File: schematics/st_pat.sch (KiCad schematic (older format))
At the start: 20 parts, among them J4 BATTERY, SW1 SW_PWR, SW2 BTN_RST, SW3 BTN, SW4 BTN, SW5 BTN, U1 FGPMMOPA6H, U2 FEATHER_M0_BASIC_PROTO, U3 LIS2MDL_ADAFRUIT, U4 Sharp_Display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

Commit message: add sharp display number to schematic
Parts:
- U4: value Sharp_Display -> Sharp_Display_4694; symbol st_pat:Sharp_Display -> st_pat:Sharp_Display_4694
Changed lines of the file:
@@
 NoConn ~ 4750 4700
 $Comp
-L st_pat:Sharp_Display U4
+L st_pat:Sharp_Display_4694 U4
 U 1 1 602ACB65
 P 8900 1750
 F 0 "U4" H 9125 1865 50  0000 C CNN
-F 1 "Sharp_Display" H 9125 1774 50  0000 C CNN
+F 1 "Sharp_Display_4694" H 9125 1774 50  0000 C CNN
 F 2 "st_pat:Sharp_Display" H 8900 1750 50  0001 C CNN
 F 3 "" H 8900 1750 50  0001 C CNN

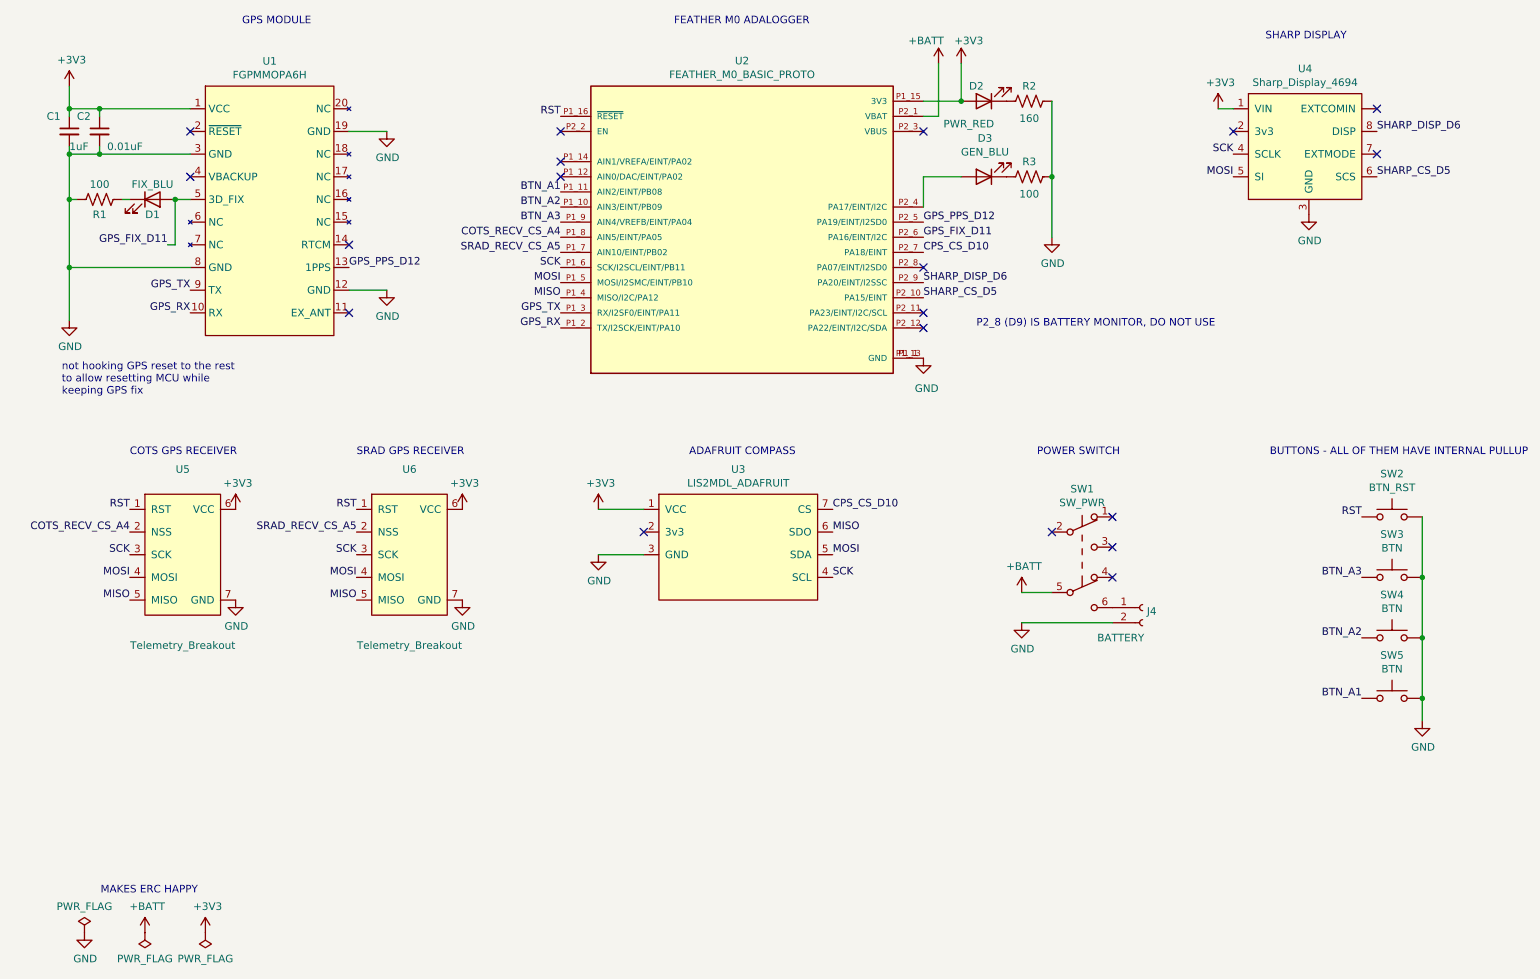
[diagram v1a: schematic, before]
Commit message: add power estimate to each component
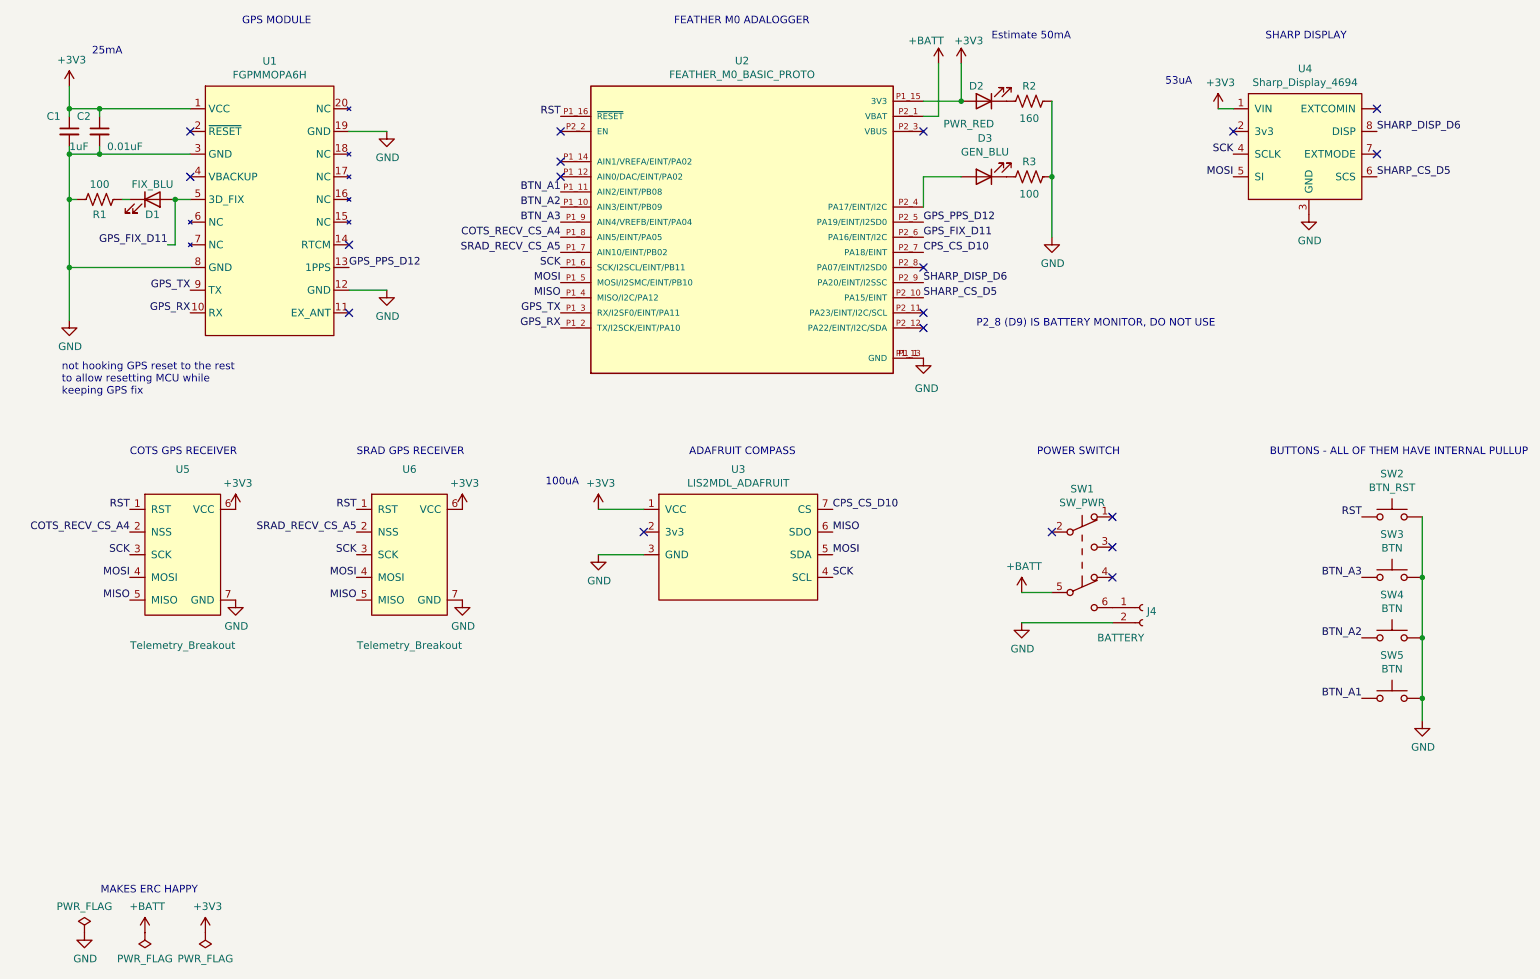
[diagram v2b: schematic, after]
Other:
- note added: "100uA"
- note added: "25mA"
- note added: "53uA"
- note added: "Estimate 50mA"
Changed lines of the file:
@@
 Text Notes 6950 3350 0    50   ~ 0
 P2_8 (D9) IS BATTERY MONITOR, DO NOT USE
+Text Notes 1100 1550 0    50   ~ 0
+25mA
+Text Notes 7050 1450 0    50   ~ 0
+Estimate 50mA
+Text Notes 8200 1750 0    50   ~ 0
+53uA
+Text Notes 4100 4400 0    50   ~ 0
+100uA
 $EndSCHEMATC

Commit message: fix pr issues
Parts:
- U5: value Telemetry_Breakout -> COTS_GPS_RECEIVER
- U6: value Telemetry_Breakout -> SRAD_GPS_RECEIVER
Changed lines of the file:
@@
 P 1700 4350
 F 0 "U5" H 1700 4415 50  0000 C CNN
-F 1 "Telemetry_Breakout" H 1700 3250 50  0000 C CNN
+F 1 "COTS_GPS_RECEIVER" H 1700 3250 50  0000 C CNN
 F 2 "st_pat:Telemetry_Breakout" H 1700 4350 50  0001 C CNN
 F 3 "" H 1700 4350 50  0001 C CNN
@@
 P 3200 4350
 F 0 "U6" H 3200 4415 50  0000 C CNN
-F 1 "Telemetry_Breakout" H 3200 3250 50  0000 C CNN
+F 1 "SRAD_GPS_RECEIVER" H 3200 3250 50  0000 C CNN
 F 2 "st_pat:Telemetry_Breakout" H 3200 4350 50  0001 C CNN
 F 3 "" H 3200 4350 50  0001 C CNN

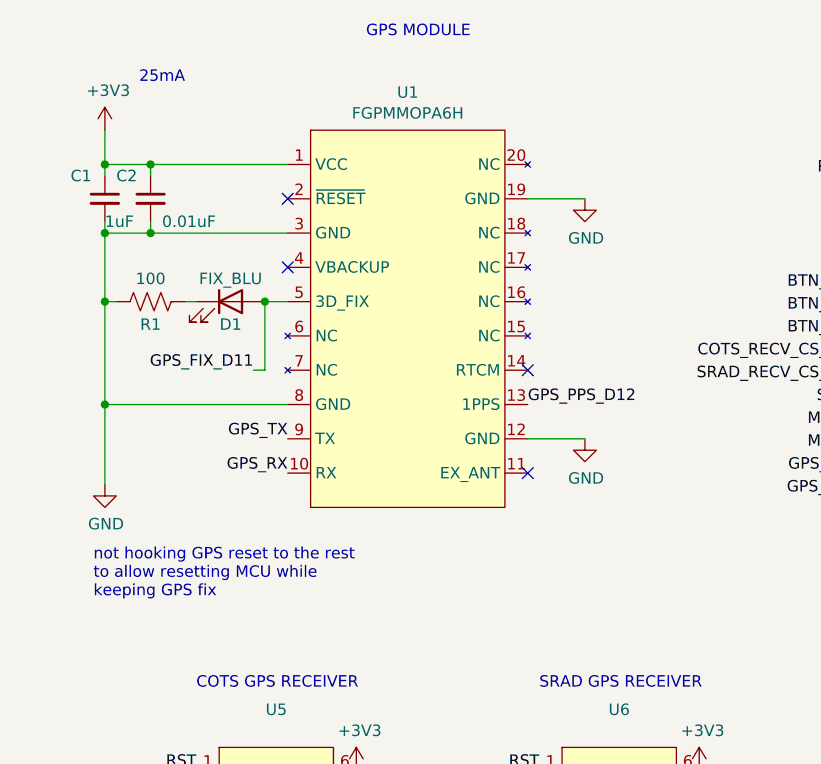
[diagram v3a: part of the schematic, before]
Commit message: wip replacing gps module with breakout
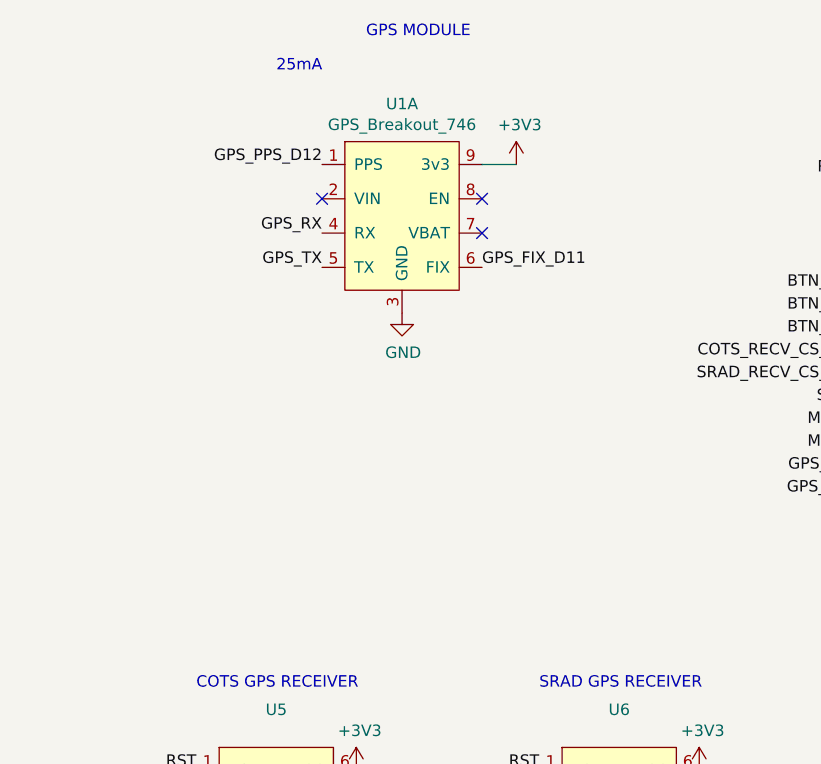
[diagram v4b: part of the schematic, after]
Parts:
- removed C1: 1uF, Capacitor_SMD:C_0805_2012Metric_Pad1.18x1.45mm_HandSolder, symbol Device:C_Small
- removed C2: 0.01uF, Capacitor_SMD:C_0805_2012Metric_Pad1.18x1.45mm_HandSolder, symbol Device:C_Small
- removed D1: FIX_BLU, LED_SMD:LED_1206_3216Metric_Pad1.42x1.75mm_HandSolder, symbol Device:LED
- removed R1: 100, Resistor_SMD:R_0805_2012Metric_Pad1.20x1.40mm_HandSolder, symbol Device:R_US
- removed U1: FGPMMOPA6H, st_pat:FGPMMOPA6H, symbol st_pat:FGPMMOPA6H
- added U1: GPS_Breakout_746, st_pat:GPS_Breakout_746, symbol st_pat:GPS_Breakout_746
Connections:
- net +3V3: now also U1.9 (3v3)
- net GND: now also U1.3 (GND)
- net GPS_FIX_D11: now also U1.6 (FIX)
- net GPS_PPS_D12: now also U1.1 (PPS)
- net GPS_RX: now also U1.4 (RX)
- net GPS_TX: now also U1.5 (TX)
- no-connect marks 19 -> 18
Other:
- note removed: "not hooking GPS reset to the rest\nto allow resetting MCU while\nkeeping GPS fix"
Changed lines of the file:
@@
 Comment4 ""
 $EndDescr
-$Comp
-L st_pat:FGPMMOPA6H U1
-U 1 1 600D122C
-P 2200 1650
-F 0 "U1" H 2275 1715 50  0000 C CNN
-F 1 "FGPMMOPA6H" H 2275 1624 50  0000 C CNN
-F 2 "st_pat:FGPMMOPA6H" H 2200 1650 50  0001 C CNN
-F 3 "https://cdn-shop.adafruit.com/datasheets/GlobalTop-FGPMMOPA6H-Datasheet-V0A.pdf" H 2200 1650 50  0001 C CNN
-	1    2200 1650
-	1    0    0    -1
-$EndComp
 Text Notes 9400 1450 2    50   ~ 0
 SHARP DISPLAY
@@
 L power:+3V3 #PWR01
 U 1 1 60185239
-P 950 1750
-F 0 "#PWR01" H 950 1600 50  0001 C CNN
-F 1 "+3V3" H 965 1923 50  0000 C CNN
-F 2 "" H 950 1750 50  0001 C CNN
-F 3 "" H 950 1750 50  0001 C CNN
-	1    950  1750
+P 2750 1900
+F 0 "#PWR01" H 2750 1750 50  0001 C CNN
+F 1 "+3V3" H 2765 2073 50  0000 C CNN
+F 2 "" H 2750 1900 50  0001 C CNN
+F 3 "" H 2750 1900 50  0001 C CNN
+	1    2750 1900
 	1    0    0    -1
 $EndComp
@@
 L power:GND #PWR03
 U 1 1 60187238
-P 950 3300
-F 0 "#PWR03" H 950 3050 50  0001 C CNN
-F 1 "GND" H 955 3127 50  0000 C CNN
-F 2 "" H 950 3300 50  0001 C CNN
-F 3 "" H 950 3300 50  0001 C CNN
-	1    950  3300
-	1    0    0    -1
-$EndComp
-$Comp
-L power:GND #PWR05
-U 1 1 60187F6E
-P 3050 2050
-F 0 "#PWR05" H 3050 1800 50  0001 C CNN
-F 1 "GND" H 3055 1877 50  0000 C CNN
-F 2 "" H 3050 2050 50  0001 C CNN
-F 3 "" H 3050 2050 50  0001 C CNN
-	1    3050 2050
-	1    0    0    -1
-$EndComp
-Wire Wire Line
-	3050 2050 2800 2050
-$Comp
-L power:GND #PWR06
-U 1 1 601889EB
-P 3050 3100
-F 0 "#PWR06" H 3050 2850 50  0001 C CNN
-F 1 "GND" H 3055 2927 50  0000 C CNN
-F 2 "" H 3050 3100 50  0001 C CNN
-F 3 "" H 3050 3100 50  0001 C CNN
-	1    3050 3100
-	1    0    0    -1
-$EndComp
-Wire Wire Line
-	3050 3100 2800 3100
-NoConn ~ 2800 2800
+P 2250 2550
+F 0 "#PWR03" H 2250 2300 50  0001 C CNN
+F 1 "GND" H 2255 2377 50  0000 C CNN
+F 2 "" H 2250 2550 50  0001 C CNN
+F 3 "" H 2250 2550 50  0001 C CNN
+	1    2250 2550
+	1    0    0    -1
+$EndComp
 $Comp
 L power:GND #PWR014
@@
 Text Label 4200 1950 2    50   ~ 0
 RST
-Wire Wire Line
-	950  1900 950  1750
-Wire Wire Line
-	1750 2200 1150 2200
-NoConn ~ 2800 3250
-NoConn ~ 1750 2350
-$Comp
-L Device:C_Small C1
-U 1 1 601E1CF3
-P 950 2050
-F 0 "C1" H 800 2150 50  0000 L CNN
-F 1 "1uF" H 950 1950 50  0000 L CNN
-F 2 "Capacitor_SMD:C_0805_2012Metric_Pad1.18x1.45mm_HandSolder" H 950 2050 50  0001 C CNN
-F 3 "~" H 950 2050 50  0001 C CNN
-	1    950  2050
-	1    0    0    -1
-$EndComp
-$Comp
-L Device:C_Small C2
-U 1 1 601E34E0
-P 1150 2050
-F 0 "C2" H 1000 2150 50  0000 L CNN
-F 1 "0.01uF" H 1200 1950 50  0000 L CNN
-F 2 "Capacitor_SMD:C_0805_2012Metric_Pad1.18x1.45mm_HandSolder" H 1150 2050 50  0001 C CNN
-F 3 "~" H 1150 2050 50  0001 C CNN
-	1    1150 2050
-	1    0    0    -1
-$EndComp
-Wire Wire Line
-	950  1900 950  1950
-Wire Wire Line
-	1150 1950 1150 1900
-Wire Wire Line
-	1150 1900 950  1900
-Wire Wire Line
-	1150 2150 1150 2200
-Wire Wire Line
-	1150 2200 950  2200
-Wire Wire Line
-	950  2150 950  2200
-Wire Wire Line
-	950  3300 950  2950
-Wire Wire Line
-	950  2950 1750 2950
-Connection ~ 950  2950
-Connection ~ 950  2200
 Text Label 8650 2200 2    50   ~ 0
 SCK
@@
 Text Label 9600 2050 0    50   ~ 0
 SHARP_DISP_D6
-Text Label 2800 2950 0    50   ~ 0
-GPS_PPS_D12
-Text Label 1750 3250 2    50   ~ 0
-GPS_RX
-Text Label 1600 2800 2    50   ~ 0
-GPS_FIX_D11
-Text Label 1750 3100 2    50   ~ 0
-GPS_TX
-Connection ~ 1150 1900
-Connection ~ 1150 2200
 Text Label 6000 4550 0    50   ~ 0
 CPS_CS_D10
@@
 	0    -1   -1   0
 $EndComp
-Wire Wire Line
-	1150 1900 1750 1900
-Connection ~ 950  1900
 Text Notes 10600 4200 2    50   ~ 0
 BUTTONS - ALL OF THEM HAVE INTERNAL PULLUP
-Wire Wire Line
-	1750 2500 1650 2500
-$Comp
-L Device:LED D1
-U 1 1 60235515
-P 1500 2500
-F 0 "D1" H 1500 2400 50  0000 C CNN
-F 1 "FIX_BLU" H 1500 2600 50  0000 C CNN
-F 2 "LED_SMD:LED_1206_3216Metric_Pad1.42x1.75mm_HandSolder" H 1500 2500 50  0001 C CNN
-F 3 "~" H 1500 2500 50  0001 C CNN
-	1    1500 2500
-	1    0    0    -1
-$EndComp
-Wire Wire Line
-	1350 2500 1300 2500
-$Comp
-L Device:R_US R1
-U 1 1 60234526
-P 1150 2500
-F 0 "R1" V 1250 2500 50  0000 C CNN
-F 1 "100" V 1050 2500 50  0000 C CNN
-F 2 "Resistor_SMD:R_0805_2012Metric_Pad1.20x1.40mm_HandSolder" V 1190 2490 50  0001 C CNN
-F 3 "~" H 1150 2500 50  0001 C CNN
-	1    1150 2500
-	0    1    1    0
-$EndComp
-Wire Wire Line
-	950  2200 950  2500
-Wire Wire Line
-	1000 2500 950  2500
-Connection ~ 950  2500
-Wire Wire Line
-	950  2500 950  2950
-Wire Wire Line
-	1650 2800 1650 2500
-Connection ~ 1650 2500
-Wire Wire Line
-	1650 2800 1600 2800
 Text Label 9500 5800 2    50   ~ 0
 BTN_A1
@@
 Text Label 1350 4550 2    50   ~ 0
 RST
-NoConn ~ 1750 2050
 Text Label 6600 2850 0    50   ~ 0
 CPS_CS_D10
 NoConn ~ 6600 3250
 NoConn ~ 6600 3350
-Text Notes 900  3800 0    50   ~ 0
-not hooking GPS reset to the rest\nto allow resetting MCU while\nkeeping GPS fix
 Text Notes 6950 3350 0    50   ~ 0
 P2_8 (D9) IS BATTERY MONITOR, DO NOT USE
-Text Notes 1100 1550 0    50   ~ 0
+Text Notes 1700 1500 0    50   ~ 0
 25mA
 Text Notes 7050 1450 0    50   ~ 0
@@
 Text Notes 4100 4400 0    50   ~ 0
 100uA
+$Comp
+L st_pat:GPS_Breakout_746 U1
+U 1 1 60E458B0
+P 2250 1750
+F 0 "U1" H 2250 1865 50  0000 C CNN
+F 1 "GPS_Breakout_746" H 2250 1774 50  0000 C CNN
+F 2 "st_pat:GPS_Breakout_746" H 2250 1750 50  0001 C CNN
+F 3 "" H 2250 1750 50  0001 C CNN
+	1    2250 1750
+	1    0    0    -1
+$EndComp
+Text Label 1900 1900 2    50   ~ 0
+GPS_PPS_D12
+Text Label 2600 2350 0    50   ~ 0
+GPS_FIX_D11
+Text Label 1900 2350 2    50   ~ 0
+GPS_TX
+Text Label 1900 2200 2    50   ~ 0
+GPS_RX
+Wire Wire Line
+	2750 1900 2600 1900
+NoConn ~ 1900 2050
+NoConn ~ 2600 2200
+NoConn ~ 2600 2050
 $EndSCHEMATC

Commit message: wip: redo layout and use diffrent button footprint
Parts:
- SW2, SW3, SW4, SW5: footprint st_pat:SW_Mini_Soft -> Button_Switch_THT:SW_PUSH_6mm
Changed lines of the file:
@@
 F 0 "SW3" H 9700 5285 50  0000 C CNN
 F 1 "BTN" H 9700 5194 50  0000 C CNN
-F 2 "st_pat:SW_Mini_Soft" H 9700 5200 50  0001 C CNN
+F 2 "Button_Switch_THT:SW_PUSH_6mm" H 9700 5200 50  0001 C CNN
 F 3 "~" H 9700 5200 50  0001 C CNN
 	1    9700 5000
@@
 F 0 "SW4" H 9700 5685 50  0000 C CNN
 F 1 "BTN" H 9700 5594 50  0000 C CNN
-F 2 "st_pat:SW_Mini_Soft" H 9700 5600 50  0001 C CNN
+F 2 "Button_Switch_THT:SW_PUSH_6mm" H 9700 5600 50  0001 C CNN
 F 3 "~" H 9700 5600 50  0001 C CNN
 	1    9700 5400
@@
 F 0 "SW5" H 9700 6085 50  0000 C CNN
 F 1 "BTN" H 9700 5994 50  0000 C CNN
-F 2 "st_pat:SW_Mini_Soft" H 9700 6000 50  0001 C CNN
+F 2 "Button_Switch_THT:SW_PUSH_6mm" H 9700 6000 50  0001 C CNN
 F 3 "~" H 9700 6000 50  0001 C CNN
 	1    9700 5800
@@
 F 0 "SW2" H 9700 4885 50  0000 C CNN
 F 1 "BTN_RST" H 9700 4794 50  0000 C CNN
-F 2 "st_pat:SW_Mini_Soft" H 9700 4800 50  0001 C CNN
+F 2 "Button_Switch_THT:SW_PUSH_6mm" H 9700 4800 50  0001 C CNN
 F 3 "~" H 9700 4800 50  0001 C CNN
 	1    9700 4600

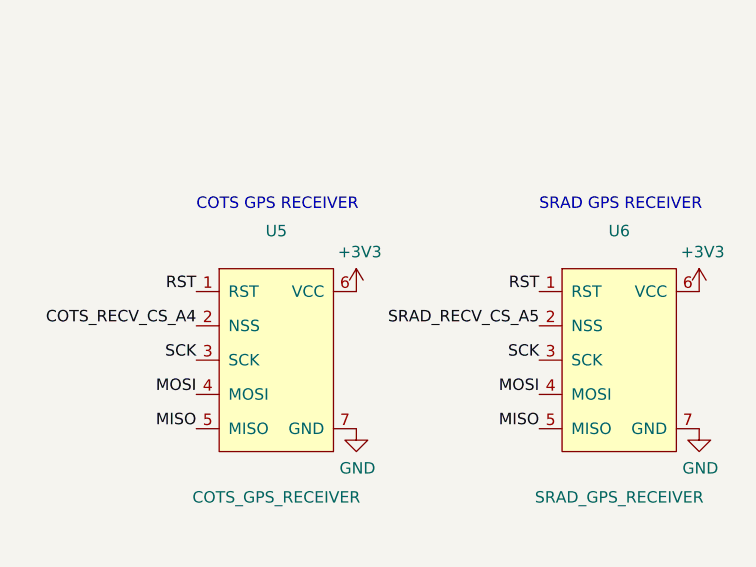
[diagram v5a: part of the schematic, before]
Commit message: update buttons layout and redo traces; add 3d model for adafruit feather
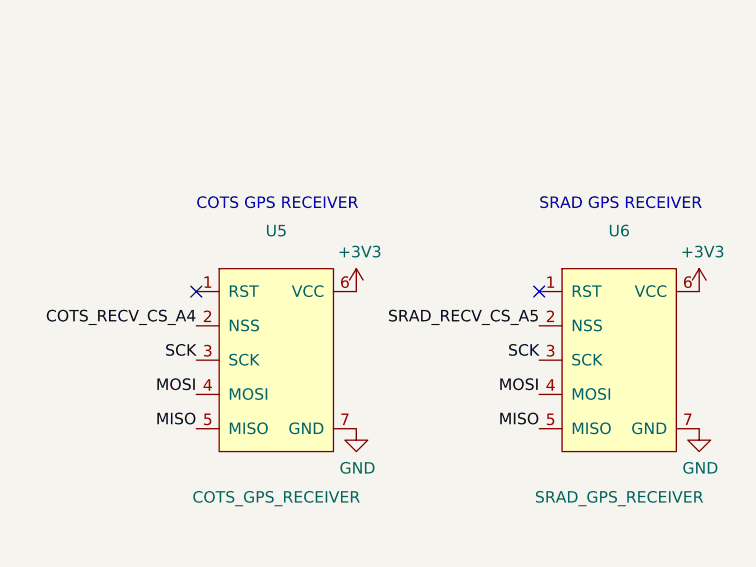
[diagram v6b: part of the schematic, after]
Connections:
- net RST: no longer U5.1 (RST), U6.1 (RST)
- no-connect marks 18 -> 20
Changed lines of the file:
@@
 MISO
 NoConn ~ 6600 2950
-Text Label 2850 4550 2    50   ~ 0
-RST
-Text Label 1350 4550 2    50   ~ 0
-RST
 Text Label 6600 2850 0    50   ~ 0
 CPS_CS_D10
@@
 NoConn ~ 2600 2200
 NoConn ~ 2600 2050
+NoConn ~ 2850 4550
+NoConn ~ 1350 4550
 $EndSCHEMATC
